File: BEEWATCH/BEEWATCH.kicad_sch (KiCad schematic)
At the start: 0 parts

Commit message: Components selections
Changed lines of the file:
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@@
 (kicad_sch (version 20230121) (generator eeschema)
   (paper "A4")
-  (sheet (at 207.01 36.576) (size 32.512 26.162) (fields_autoplaced)
+  (sheet (at 202.565 37.846) (size 32.512 26.162) (fields_autoplaced)
     (stroke (width 0.1524) (type solid))
     (fill (color 0 0 0 0.0000))
-    (property "Sheetname" "Display" (at 207.01 35.8644 0)
+    (property "Sheetname" "Display" (at 202.565 37.1344 0)
       (effects (font (size 1.27 1.27)) (justify left bottom))
     )
-    (property "Sheetfile" "Display.kicad_sch" (at 207.01 63.3226 0)
+    (property "Sheetfile" "Display.kicad_sch" (at 202.565 64.5926 0)
       (effects (font (size 1.27 1.27)) (justify left top))
     )
-    (pin "TFT_SDI" input (at 207.01 52.705 180)
+    (pin "TFT_SDI" input (at 202.565 53.975 180)
       (effects (font (size 1.27 1.27)) (justify left))
     )
-    (pin "TFT_SCK" input (at 207.01 50.165 180)
+    (pin "TFT_SCK" input (at 202.565 51.435 180)
       (effects (font (size 1.27 1.27)) (justify left))
     )
-    (pin "TFT_CS" input (at 207.01 47.625 180)
+    (pin "TFT_CS" input (at 202.565 48.895 180)
       (effects (font (size 1.27 1.27)) (justify left))
     )
-    (pin "TFT_D{slash}C" input (at 207.01 45.085 180)
+    (pin "TFT_D{slash}C" input (at 202.565 46.355 180)
       (effects (font (size 1.27 1.27)) (justify left))
     )
-    (pin "TFT_LED_PIN" input (at 207.01 55.245 180)
+    (pin "TFT_LED_PIN" input (at 202.565 56.515 180)
       (effects (font (size 1.27 1.27)) (justify left))
     )
-    (pin "TFT_RST" input (at 207.01 57.785 180)
+    (pin "TFT_RST" input (at 202.565 59.055 180)
       (effects (font (size 1.27 1.27)) (justify left))
     )

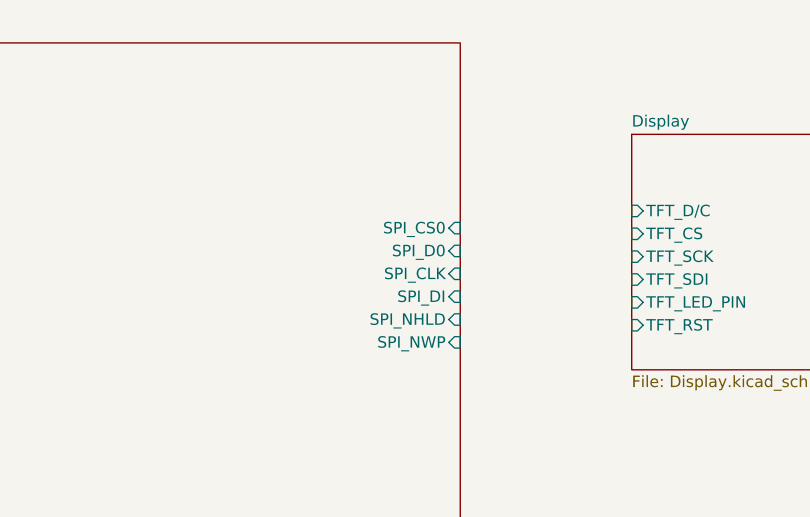
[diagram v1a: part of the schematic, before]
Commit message: Insufficient GPIOs planning to add/C MUX or MCU
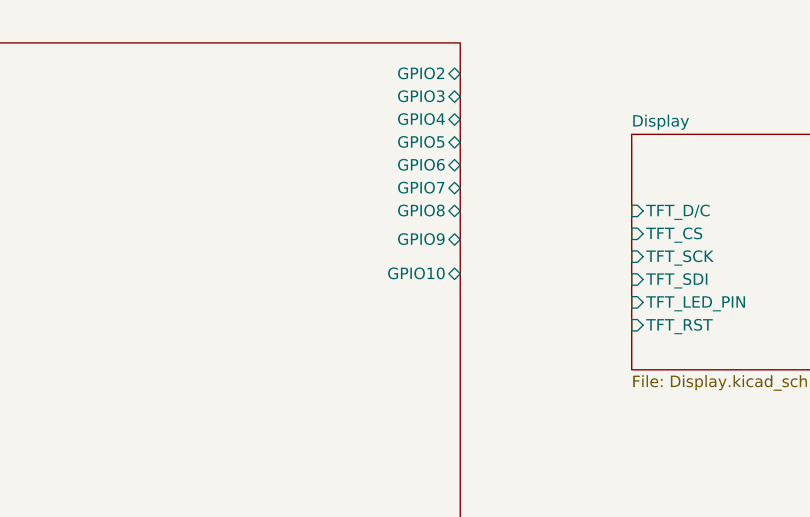
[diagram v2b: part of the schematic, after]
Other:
- sheet ESP32 ports: added GPIO10, GPIO2, GPIO3, GPIO4, GPIO5, GPIO6, GPIO7, GPIO8, GPIO9; removed SPI_CLK, SPI_CS0, SPI_D0, SPI_DI, SPI_NHLD, SPI_NWP
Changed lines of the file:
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@@
       (effects (font (size 1.27 1.27)) (justify left top))
-    )
-    (pin "SPI_CS0" input (at 183.515 48.26 0)
-      (effects (font (size 1.27 1.27)) (justify right))
-    )
-    (pin "SPI_D0" input (at 183.515 50.8 0)
-      (effects (font (size 1.27 1.27)) (justify right))
-    )
-    (pin "SPI_CLK" input (at 183.515 53.34 0)
-      (effects (font (size 1.27 1.27)) (justify right))
-    )
-    (pin "SPI_DI" input (at 183.515 55.88 0)
-      (effects (font (size 1.27 1.27)) (justify right))
-    )
-    (pin "SPI_NHLD" input (at 183.515 58.42 0)
-      (effects (font (size 1.27 1.27)) (justify right))
-    )
-    (pin "SPI_NWP" input (at 183.515 60.96 0)
-      (effects (font (size 1.27 1.27)) (justify right))
     )
     (pin "TXD" input (at 183.515 100.965 0)
@@
       (effects (font (size 1.27 1.27)) (justify right))
     )
+    (pin "GPIO6" bidirectional (at 183.515 41.275 0)
+      (effects (font (size 1.27 1.27)) (justify right))
+    )
+    (pin "GPIO7" bidirectional (at 183.515 43.815 0)
+      (effects (font (size 1.27 1.27)) (justify right))
+    )
+    (pin "GPIO4" bidirectional (at 183.515 36.195 0)
+      (effects (font (size 1.27 1.27)) (justify right))
+    )
+    (pin "GPIO8" bidirectional (at 183.515 46.355 0)
+      (effects (font (size 1.27 1.27)) (justify right))
+    )
+    (pin "GPIO5" bidirectional (at 183.515 38.735 0)
+      (effects (font (size 1.27 1.27)) (justify right))
+    )
+    (pin "GPIO2" bidirectional (at 183.515 31.115 0)
+      (effects (font (size 1.27 1.27)) (justify right))
+    )
+    (pin "GPIO3" bidirectional (at 183.515 33.655 0)
+      (effects (font (size 1.27 1.27)) (justify right))
+    )
+    (pin "GPIO9" bidirectional (at 183.515 49.53 0)
+      (effects (font (size 1.27 1.27)) (justify right))
+    )
+    (pin "GPIO10" bidirectional (at 183.515 53.34 0)
+      (effects (font (size 1.27 1.27)) (justify right))
+    )
